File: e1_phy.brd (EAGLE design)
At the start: 160 x 100 mm, 53 parts, among them U1 XRT82D20, X1 RJ45-8L-B, X2 MINI-USB-32005-201

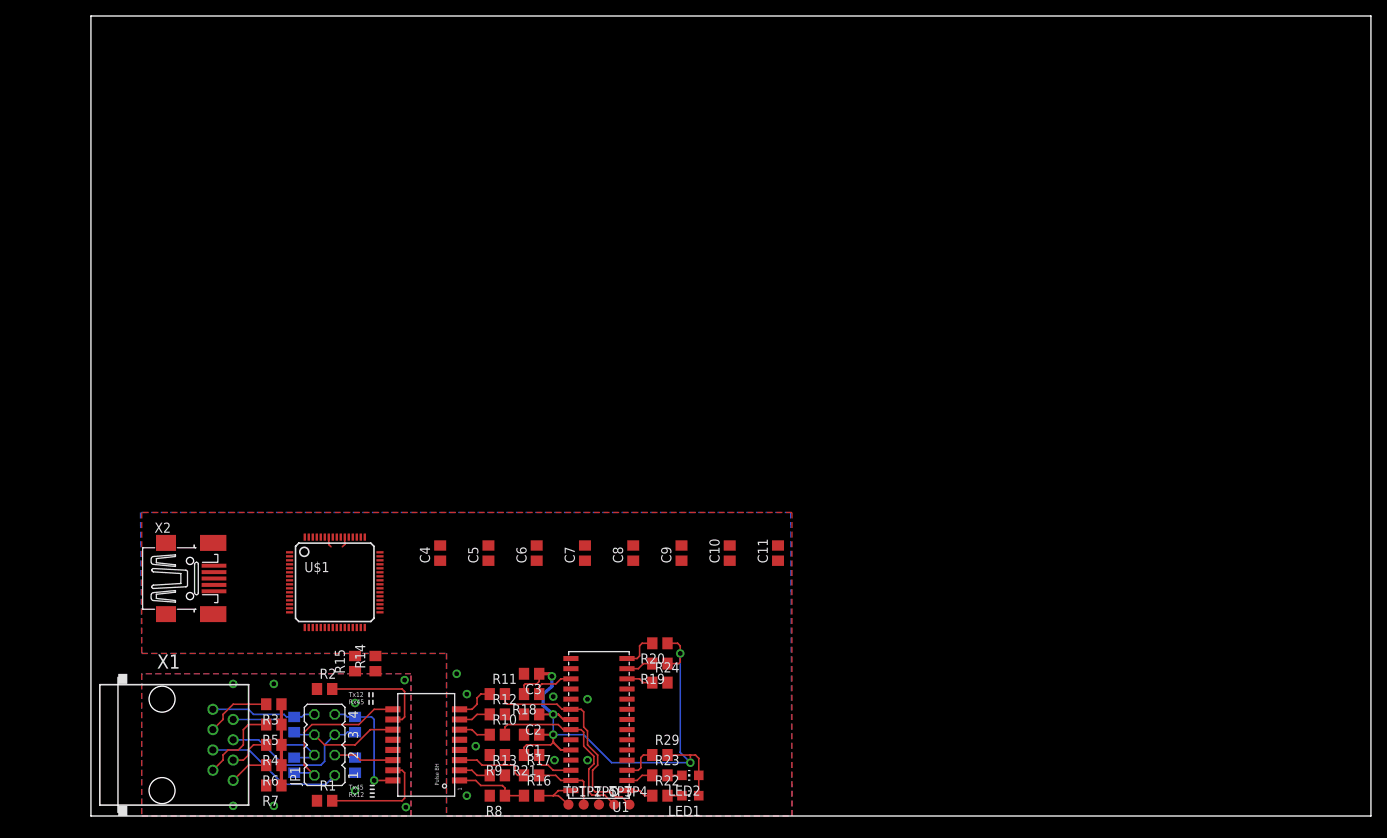
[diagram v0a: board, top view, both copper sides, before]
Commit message: First sane version, for review.
I've smashed all the random edits and redesigns into this single commit,
the history was not useful to keep.
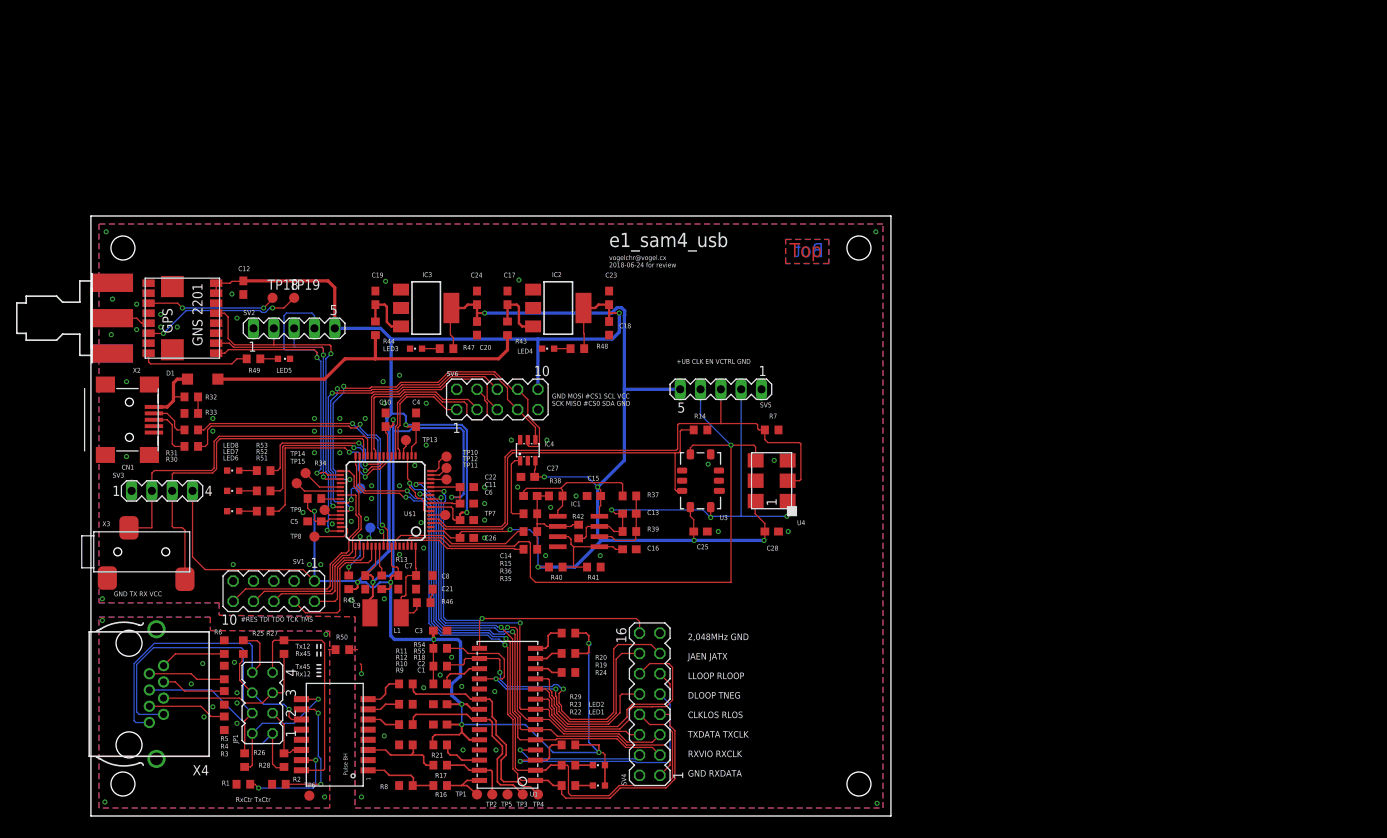
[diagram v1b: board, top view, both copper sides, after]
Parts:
- removed X1: RJ45-8L-B, con-tycoelectronics:RJ45-NO-SHIELD
- added C12, C13, C14, C15, C16, C17, C18, C19, C20, C25, C26, C27, C28: 100n, rcl:C0603
- added C21, C22, C23, C24: 10uF, rcl:C0603
- added CN1: (no value), adafruit:USB-MINIB
- added D1: MBR0520LT, diode:SOD123
- added IC1: (no value), linear:SO08
- added IC2, IC3: LD117AS33TR, v-reg:SOT223
- added IC4: MCP4725, dp_devices:SOT-23-6
- added L1: 10uH, rcl:L1812
- added LED3, LED4, LED5, LED6, LED7, LED8: (no value), led:CHIPLED_0603
- added R30, R31: 33R, rcl:R0603
- added R32: 27k, rcl:R0603
- added R33: 47k, rcl:R0603
- added R34, R50: DNP, rcl:R0603
- added R35: 680k, rcl:R0603
- added R36, R37, R38, R39, R40, R41: 10k, rcl:R0603
- added R42: 0R (DNP), rcl:R0603
- added R43, R44: BLM/0R, rcl:R0603
- added R45: 0R, rcl:R0603
- added R46: 1R, rcl:R0603
- added R47, R48, R49, R51, R52, R53, R54, R55: 1k, rcl:R0603
- added SV1, SV6: (no value), con-lstb:MA05-2
- added SV2, SV5: (no value), con-lstb:MA05-1
- added SV3: (no value), con-lstb:MA04-1
- added SV4: (no value), con-lstb:MA08-2
- added TP10, TP11, TP12, TP13, TP14, TP15, TP16, TP17, TP18, TP19, TP6, TP7, TP8, TP9: TPB1,27, testpad:B1,27
- added U2: GPS_GNS_2201, cvogel:GPS_GNS_2201
- added U3: VCTCXO-CONNORWINFIELD, Connor-Winfield_VCTCXO:VCTCXO-CONNORWINFIELD
- added U4: VCXO_TAITIEN_VT, cvogel:VCXO_TAITIEN_VT_7MM_5MM
- added X3: JACK2.5_SJ-2523, SJ-2523-JACK:JACK2.5_SJ-2523
- added X4: 0446200002, con-molex:0446200002
- C1, C10, C11, C2, C3, C4, C5, C6, C7, C8, C9: device rcl:C0805 -> rcl:C0603
- LED1, LED2: device led:CHIP-LED0805 -> led:CHIPLED_0603
- R1, R10, R11, R12, R16, R17, R18, R19, R2, R20, R21, R22, R23, R24, R25, R26, R27, R28, R29, R8, R9: device rcl:R0805 -> rcl:R0603
- R13: value 0R -> DNP; device rcl:R0805 -> rcl:R0603
- R14: value DNP -> 10k; device rcl:R0805 -> rcl:R0603
- R15: value ? -> 10k; device rcl:C0805 -> rcl:R0603
- R3, R4, R5, R6: value 60R -> DNP; device rcl:R0805 -> rcl:R0603
- R7: value 0R -> 10k; device rcl:R0805 -> rcl:R0603
- X2: value MINI-USB-32005-201 -> SMA-142-0701-801/806; device con-cypressindustries:32005-201 -> con-coax:J502-ND-142-0701-801/806
- moved R7 76.5 mm to (85.1, 48.3)
- moved R14 50.0 mm to (76.2, 48.3), turned to 0 degrees
- moved C10 46.1 mm to (36.8, 49.5)
- moved C9 39.7 mm to (34.3, 29.2), turned to 270 degrees
- moved C11 39.4 mm to (47.0, 39.1), turned to 0 degrees
- moved X2 34.8 mm to (0.16, 62.2)
- moved R15 28.8 mm to (54.9, 37.8), turned to 0 degrees
- moved R13 28.1 mm to (36.4, 29.2), turned to 90 degrees
- moved C8 27.4 mm to (40.6, 29.2), turned to 270 degrees
- moved C7 23.6 mm to (38.4, 29.2), turned to 270 degrees
- moved C5 22.1 mm to (27.9, 36.8), turned to 180 degrees
- moved C4 16.9 mm to (40.6, 49.5)
- moved R6 16.0 mm to (16.7, 21.1), turned to 270 degrees
- moved R2 13.2 mm to (23.5, 3.97)
- moved R27 13.1 mm to (24.1, 21.1), flipped to the top
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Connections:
- removed net N$3: R29.1, U1.3
- removed net RX_SEC_CTR: R13.1, TR1.2
- new net #GPS_RESET: TP18.TP, U2.3
- new net #RESET: SV1.10, U$1.39
- new net #SPI_CS0: SV6.5, U$1.28
- new net #SPI_CS1: SV6.6, U$1.42
- new net +UB: C15.1, C20.1, C24.1, C25.2, C26.2, C27.2, C28.2, IC1.8, IC3.4, IC4.3, R40.1, R47.2, SV5.5, U$1.1, U3.9, U4.6
- new net +UB_HALF: C16.2, IC1.3, IC1.5, R40.2, R41.2
- new net DAC0: R36.1, U$1.59
- new net DAC1: R35.1, U$1.63
- new net DAC_I2C: IC4.1, R15.1
- new net GPS_PPS: SV2.2, U$1.48, U2.13
- new net GPS_SAM4_RX: SV2.3, U$1.35, U2.10
- new net GPS_SAM4_TX: SV2.4, U$1.34, U2.9
- new net I2C_SCL: IC4.5, SV6.8, U$1.36
- new net I2C_SDA: IC4.4, SV6.7, U$1.43
- new net JTAGSEL: R45.2, U$1.50
- new net LED1: R51.2, U$1.23
- new net LED2: R52.2, U$1.25
- new net LED3: R53.2, U$1.26
- new net LINE_PIN3: R3.2, X4.3
- new net LINE_PIN6: R4.2, X4.6
- new net LINE_PIN7: R5.2, X4.7
- new net LINE_PIN8: R6.2, X4.8
- new net N$10: R49.2, U2.8
- new net N$11: LED5.A, R49.1
- new net N$12: CN1.VBUS, D1.A, R32.2
- new net N$13: C19.1, IC3.3, R44.1
- new net N$14: C17.1, IC2.3, R43.1
- new net N$15: C21.1, R46.1
- new net N$16: LED3.A, R47.1
- new net N$17: TP16.TP, U$1.41
- new net N$18: LED4.A, R48.1
- new net N$19: TP12.TP, U$1.15
- new net N$20: TP13.TP, U$1.20
- new net N$21: TP7.TP, U$1.5
- new net N$22: TP14.TP, U$1.37
- new net N$23: TP15.TP, U$1.38
- new net N$24: TP19.TP, U2.6
- new net N$26: LED6.A, R51.1
- new net N$27: LED7.A, R52.1
- new net N$28: LED8.A, R53.1
- new net N$4: U2.5, X2.1
- new net OPAMP1_IN_NEG: C14.1, IC1.2, R15.2, R35.2, R36.2, R38.1, R42.1
- new net OPAMP1_OUT: C14.2, IC1.1, R37.1, R38.2
- new net OPAMP2_IN_NEG: C13.1, IC1.6, R37.2, R39.1
- new net PB12_ERASE: R13.2, U$1.55
- new net SAM4S_CLK: SV5.4, U$1.62, U3.5, U4.4
- new net SPI_MISO: SV6.3, U$1.27
- new net SPI_MOSI: SV6.4, U$1.22
- new net SPI_SCK: SV6.1, U$1.21
- new net TCK_SWDCLK: SV1.4, U$1.53
- new net TDI: SV1.8, U$1.33
- new net TDO: SV1.6, U$1.49
- new net TMS_SWDIO: SV1.2, U$1.51
- new net TNEG_CODE: R29.1, SV4.9, U1.3
- new net TST: R34.2, U$1.40
- new net URXD0_SAMBA_RX: SV3.3, U$1.30, X3.2
- new net USB_DDM: R31.1, U$1.56
- new net USB_DDM_CON: CN1.D-, R31.2
- new net USB_DDP: R30.1, U$1.57
- new net USB_DDP_CON: CN1.D+, R30.2
- new net USB_VBUS_CON: D1.C, R43.2, R44.2
- new net USB_VBUS_SENS: R32.1, R33.2
- new net UTXD0_SAMBA_TX: SV3.2, U$1.29, X3.3
- new net VCTCXO_EN: R14.1, U$1.3, U3.8
- new net VCXO_CTRL: C13.2, IC1.7, R39.2, R42.2, SV5.2, U3.10, U4.1
- new net VCXO_EN: R7.2, SV5.3, U$1.4, U4.2
- new net VDDCORE: C10.1, C11.1, C22.1, C9.1, L1.2, U$1.12, U$1.24, U$1.54, U$1.8
- new net VDDPLL: C8.1, L1.1, R46.2, U$1.64
- net #CLKLOS: now also SV4.8, U$1.31
- net #DLOOP: now also SV4.10
- net #LLOOP: now also SV4.12
- net #RLOOP: now also SV4.11
- net #RLOS: now also SV4.7, U$1.32
- net CLK2048: now also SV4.16, U$1.11
- net GND: now also C12.2, C15.2, C16.1, C17.2, C18.2, C19.2, C20.2, C21.2, C22.2, C23.2, C24.2, C25.1, C26.1, C27.1, C28.1, CN1.GND, IC1.4, IC2.1, IC3.1, IC4.2, IC4.6, LED3.C, LED4.C, LED5.C, LED6.C, LED7.C, LED8.C, R33.1, R41.1, R50.2, R7.1, SV1.3, SV1.5, SV1.9, SV2.1, SV3.1, SV4.15, SV4.2, SV5.1, SV6.2, SV6.9, TR1.2, U2.4, U2.E1, U2.E2, U3.4, U4.3, X2.G@1, X2.G@2, X2.G@3, X2.G@4, X3.1; no longer R13.2, R15.2
- net GNDIO: now also R3.1, R4.1, R5.1, R50.1, R6.1, TP6.TP, X4.S@1, X4.S@2; no longer R14.1, R15.1, R7.2
- net JAEN: now also R54.2, SV4.14
- net JATX: now also R55.2, SV4.13
- net LINE_PIN1: now also X4.1; no longer X1.1
- net LINE_PIN2: now also X4.2; no longer X1.2
- net LINE_PIN4: now also X4.4; no longer X1.4
- net LINE_PIN5: now also X4.5; no longer X1.5
- net N$5: now also TP17.TP, U$1.52; no longer R3.2, X1.3
- net N$6: now also TP9.TP, U$1.44; no longer R4.2, X1.6
- net N$7: now also TP8.TP, U$1.47; no longer R5.2, X1.7
- net N$8: now also TP10.TP, U$1.16; no longer R6.2, X1.8
- net N$9: now also TP11.TP, U$1.14; no longer R3.1, R4.1, R5.1, R6.1, R7.1
- net RX_CLK: now also SV4.3, U$1.13
- net RX_DATA: now also SV4.1, U$1.10
- net RX_VIOLATION: now also SV4.4
- net TX_CLK: now also SV4.5, U$1.19, U$1.6
- net TX_DATA: now also SV4.6, U$1.9
- net VCC: now also C12.1, C18.1, C23.1, IC2.4, R13.1, R34.1, R45.1, R48.2, R54.1, R55.1, SV1.1, SV2.5, SV3.4, SV6.10, U$1.7, U2.15, U2.16; no longer C10.1, C11.1, C8.1, C9.1, U$1.12, U$1.24, U$1.54
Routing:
- net VCC: track 79.5 -> 301.4 mm, vias 5 -> 11
- net +UB: track 0.00 -> 140.7 mm, vias 0 -> 7
- net #CLKLOS: track 3.43 -> 90.4 mm, vias 0 -> 2
- net #RLOS: track 3.43 -> 88.3 mm, vias 0 -> 2
- net SAM4S_CLK: track 0.00 -> 83.2 mm, vias 0 -> 1
- net VCXO_EN: track 0.00 -> 71.1 mm
- net TX_CLK: track 0.00 -> 68.9 mm, vias 0 -> 2
- net VDDCORE: track 0.00 -> 66.5 mm, vias 0 -> 3
- net RX_DATA: track 0.00 -> 65.0 mm, vias 0 -> 2
- net RX_CLK: track 0.00 -> 61.9 mm, vias 0 -> 2
- net TX_DATA: track 0.00 -> 54.1 mm, vias 0 -> 2
- net VCXO_CTRL: track 0.00 -> 52.3 mm, vias 0 -> 3
- net VCTCXO_EN: track 0.00 -> 50.2 mm
- net I2C_SDA: track 0.00 -> 49.7 mm, vias 0 -> 2
- net I2C_SCL: track 0.00 -> 49.4 mm, vias 0 -> 2
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- added copper zone on layer 1, net N$3
- added copper zone on layer 16, net N$3
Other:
- board size 160 x 100 mm -> 100 x 75 mm
- board text added: "#RES TDI TDO TCK TMS"
- board text added: "+UB CLK EN VCTRL GND"
- board text added: "2,048MHz GND JAEN JATX LLOOP RLOOP DLOOP TNEG CLKLOS RLOS TXDATA TXCLK RXVIO RXCLK GND RXDATA"
- board text added: "Bot"
- board text added: "GND MOSI #CS1 SCL VCC SCK MISO #CS0 SDA GND"
- board text added: "GND TX RX VCC"
- board text added: "RxCtr TxCtr"
- board text added: "Top"
- board text added: "e1_sam4_usb"
- board text added: "vogelchr@vogel.cx 2018-06-24 for review"
